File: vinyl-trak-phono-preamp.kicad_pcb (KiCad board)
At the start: 2 copper layers, 64 x 31.5 mm, 67 parts, among them J2 Screw_Terminal_01x03, J3 Screw_Terminal_01x02, J4 Screw_Terminal_01x02, Q1 2N3906, Q10 2N3906, Q11 JFE2140D, Q12 2N5089, Q13 2N3904, Q14 2N3904, Q15 2N5089, Q16 2N5087, Q17 2N5087, Q18 2N5089, Q19 2N5089, Q2 2N3904, Q20 2N5087, Q21 2N5089, Q3 2N3906, Q4 2N3906, Q5 2N3904, Q6 2N3904, Q7 2N3904, Q8 2N3906, Q9 2N3904, U1 OPA2134

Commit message: Revision 0.1
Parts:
- removed J2: Screw_Terminal_01x03, TerminalBlock_4Ucon:TerminalBlock_4Ucon_1x03_P3.50mm_Horizontal
- removed J3: Screw_Terminal_01x02, TerminalBlock_4Ucon:TerminalBlock_4Ucon_1x02_P3.50mm_Horizontal
- removed R38: 1, Resistor_SMD:R_0805_2012Metric_Pad1.20x1.40mm_HandSolder
- added C10: 100p, Capacitor_SMD:C_0805_2012Metric_Pad1.18x1.45mm_HandSolder, F.Cu at (74.9, 96.4)
- added C13: 0.015u, Capacitor_SMD:C_0805_2012Metric_Pad1.18x1.45mm_HandSolder, F.Cu at (104.0, 102.1)
- added C14: .47u, Capacitor_SMD:C_1206_3216Metric_Pad1.33x1.80mm_HandSolder, F.Cu at (129.5, 96.5)
- added C15: 10n, Capacitor_SMD:C_0805_2012Metric_Pad1.18x1.45mm_HandSolder, F.Cu at (125.0, 96.7)
- added C16: 10n, Capacitor_SMD:C_0805_2012Metric_Pad1.18x1.45mm_HandSolder, F.Cu at (129.4, 101.8)
- added C17: 0.020u, Capacitor_SMD:C_0805_2012Metric_Pad1.18x1.45mm_HandSolder, F.Cu at (124.8, 108.4)
- added C19: .47u, Capacitor_SMD:C_1206_3216Metric_Pad1.33x1.80mm_HandSolder, F.Cu at (130.5, 58.7)
- added C20: .47u, Capacitor_SMD:C_1206_3216Metric_Pad1.33x1.80mm_HandSolder, F.Cu at (129.5, 94.0)
- added D3: 1N4148W, Diode_SMD:D_SOD-123F, F.Cu at (132.7, 98.9)
- added D4: 1N4148W, Diode_SMD:D_SOD-123F, F.Cu at (132.8, 101.2)
- added J11: Screw_Terminal_01x02, Library:TerminalBlock_4Ucon_1x02_P5mm_Horizontal, F.Cu at (140.2, 91.6)
- added J12: Screw_Terminal_01x02, Library:TerminalBlock_4Ucon_1x02_P5mm_Horizontal, F.Cu at (75.9, 107.1)
- added J13: Screw_Terminal_01x02, Library:TerminalBlock_4Ucon_1x02_P5mm_Horizontal, F.Cu at (77.0, 71.6)
- added J7: Screw_Terminal_01x02, Library:TerminalBlock_4Ucon_1x02_P5mm_Horizontal, F.Cu at (132.5, 117.7)
- added J8: Screw_Terminal_01x02, Library:TerminalBlock_4Ucon_1x02_P5mm_Horizontal, F.Cu at (76.2, 90.5)
- added Q22: 2N3906, Library:SOT-23_Handsoldering-adjusted-pinout, F.Cu at (107.1, 90.4)
- added Q23: 2N3904, Library:SOT-23_Handsoldering-adjusted-pinout, F.Cu at (109.7, 117.1)
- added Q24: 2N3906, Library:SOT-23_Handsoldering-adjusted-pinout, F.Cu at (108.9, 95.4)
- added Q25: 2N3906, Library:SOT-23_Handsoldering-adjusted-pinout, F.Cu at (109.9, 100.8)
- added Q26: 2N3904, Library:SOT-23_Handsoldering-adjusted-pinout, F.Cu at (109.7, 104.4)
- added Q27: 2N3904, Library:SOT-23_Handsoldering-adjusted-pinout, F.Cu at (109.7, 112.0)
- added Q28: 2N3904, Library:SOT-23_Handsoldering-adjusted-pinout, F.Cu at (116.0, 98.0)
- added Q29: 2N3906, Library:SOT-23_Handsoldering-adjusted-pinout, F.Cu at (109.7, 108.2)
- added Q30: 2N3904, Library:SOT-23_Handsoldering-adjusted-pinout, F.Cu at (118.6, 91.7)
- added Q31: 2N3906, Library:SOT-23_Handsoldering-adjusted-pinout, F.Cu at (119.8, 115.6)
- added Q32: JFE2140D, Package_SO:SOIC-8_3.9x4.9mm_P1.27mm, F.Cu at (83.0, 105.6)
- added Q33: 2N5089, Library:SOT-23_Handsoldering-adjusted-pinout, F.Cu at (91.9, 96.7)
- added Q34: 2N3904, Library:SOT-23_Handsoldering-adjusted-pinout, F.Cu at (90.4, 117.1)
- added Q35: 2N3904, Library:SOT-23_Handsoldering-adjusted-pinout, F.Cu at (85.0, 113.0)
- added Q36: 2N5089, Library:SOT-23_Handsoldering-adjusted-pinout, F.Cu at (92.4, 104.2)
- added Q37: 2N5087, Library:SOT-23_Handsoldering-adjusted-pinout, F.Cu at (98.3, 95.5)
- added Q38: 2N5087, Library:SOT-23_Handsoldering-adjusted-pinout, F.Cu at (98.3, 105.6)
- added Q39: 2N5089, Library:SOT-23_Handsoldering-adjusted-pinout, F.Cu at (98.3, 113.2)
- added Q40: 2N5089, Library:SOT-23_Handsoldering-adjusted-pinout, F.Cu at (98.3, 109.4)
- added Q41: 2N5087, Library:SOT-23_Handsoldering-adjusted-pinout, F.Cu at (98.3, 101.8)
- added Q42: 2N5089, Library:SOT-23_Handsoldering-adjusted-pinout, F.Cu at (103.3, 106.9)
- added R32: 100k, Resistor_SMD:R_0805_2012Metric_Pad1.20x1.40mm_HandSolder, F.Cu at (82.0, 100.7)
- added R39: 18k, Resistor_SMD:R_0805_2012Metric_Pad1.20x1.40mm_HandSolder, F.Cu at (74.9, 98.6)
- added R40: 100k, Resistor_SMD:R_0805_2012Metric_Pad1.20x1.40mm_HandSolder, F.Cu at (76.1, 112.2)
- added R41: 1k37, Resistor_SMD:R_0805_2012Metric_Pad1.20x1.40mm_HandSolder, F.Cu at (102.1, 101.8)
- added R42: 205k, Resistor_SMD:R_0805_2012Metric_Pad1.20x1.40mm_HandSolder, F.Cu at (106.0, 103.3)
- added R43: 220, Resistor_SMD:R_0805_2012Metric_Pad1.20x1.40mm_HandSolder, F.Cu at (113.5, 93.9)
- added R44: 220, Resistor_SMD:R_0805_2012Metric_Pad1.20x1.40mm_HandSolder, F.Cu at (113.7, 116.7)
- added R45: 604, Resistor_SMD:R_0805_2012Metric_Pad1.20x1.40mm_HandSolder, F.Cu at (113.5, 90.1)
- added R46: 604, Resistor_SMD:R_0805_2012Metric_Pad1.20x1.40mm_HandSolder, F.Cu at (116.0, 118.1)
- added R47: 1, Resistor_SMD:R_0805_2012Metric_Pad1.20x1.40mm_HandSolder, F.Cu at (116.6, 101.8)
- added R48: 220, Resistor_SMD:R_0805_2012Metric_Pad1.20x1.40mm_HandSolder, F.Cu at (118.6, 101.8)
- added R49: 220, Resistor_SMD:R_0805_2012Metric_Pad1.20x1.40mm_HandSolder, F.Cu at (118.8, 107.8)
- added R50: 1k47, Resistor_SMD:R_0805_2012Metric_Pad1.20x1.40mm_HandSolder, F.Cu at (94.4, 90.4)
- added R52: 100, Resistor_SMD:R_0805_2012Metric_Pad1.20x1.40mm_HandSolder, F.Cu at (88.9, 100.3)
- added R53: 71k5, Resistor_SMD:R_0805_2012Metric_Pad1.20x1.40mm_HandSolder, F.Cu at (90.6, 90.4)
- added R54: 56k2, Resistor_SMD:R_0805_2012Metric_Pad1.20x1.40mm_HandSolder, F.Cu at (81.7, 118.3)
- added R55: 20.5k, Resistor_SMD:R_0805_2012Metric_Pad1.20x1.40mm_HandSolder, F.Cu at (86.8, 90.4)
- added R56: 220, Resistor_SMD:R_0805_2012Metric_Pad1.20x1.40mm_HandSolder, F.Cu at (89.1, 113.2)
- added R57: 160, Resistor_SMD:R_0805_2012Metric_Pad1.20x1.40mm_HandSolder, F.Cu at (86.6, 118.1)
- added R58: 1k47, Resistor_SMD:R_0805_2012Metric_Pad1.20x1.40mm_HandSolder, F.Cu at (98.3, 90.4)
- added R59: 100, Resistor_SMD:R_0805_2012Metric_Pad1.20x1.40mm_HandSolder, F.Cu at (88.1, 106.9)
- added R60: 56k2, Resistor_SMD:R_0805_2012Metric_Pad1.20x1.40mm_HandSolder, F.Cu at (101.0, 98.7)
- added R62: 1k47, Resistor_SMD:R_0805_2012Metric_Pad1.20x1.40mm_HandSolder, F.Cu at (129.8, 105.6)
- added R63: 1k47, Resistor_SMD:R_0805_2012Metric_Pad1.20x1.40mm_HandSolder, F.Cu at (131.8, 105.6)
- added R64: 15k0, Resistor_SMD:R_0805_2012Metric_Pad1.20x1.40mm_HandSolder, F.Cu at (127.8, 107.3)
- added R65: 162k, Resistor_SMD:R_0805_2012Metric_Pad1.20x1.40mm_HandSolder, F.Cu at (124.9, 106.4)
- added R66: 1k78, Resistor_SMD:R_0805_2012Metric_Pad1.20x1.40mm_HandSolder, F.Cu at (97.0, 118.1)
- added R67: 1Meg, Resistor_SMD:R_0805_2012Metric_Pad1.20x1.40mm_HandSolder, F.Cu at (122.0, 102.7)
- added R68: 33.2k, Resistor_SMD:R_0805_2012Metric_Pad1.20x1.40mm_HandSolder, F.Cu at (102.1, 90.4)
- added R69: 3k83, Resistor_SMD:R_0805_2012Metric_Pad1.20x1.40mm_HandSolder, F.Cu at (104.3, 110.8)
- added R70: 47.5k, Resistor_SMD:R_0805_2012Metric_Pad1.20x1.40mm_HandSolder, F.Cu at (100.8, 118.1)
- added R71: 115k, Resistor_SMD:R_0805_2012Metric_Pad1.20x1.40mm_HandSolder, F.Cu at (93.2, 118.3)
- added R72: 1k78, Resistor_SMD:R_0805_2012Metric_Pad1.20x1.40mm_HandSolder, F.Cu at (104.6, 118.1)
- added R75: 1, Resistor_SMD:R_0805_2012Metric_Pad1.20x1.40mm_HandSolder, F.Cu at (105.9, 63.2)
- added R76: 1, Resistor_SMD:R_0805_2012Metric_Pad1.20x1.40mm_HandSolder, F.Cu at (104.8, 98.6)
- added U2: OPA2134, Package_SO:SOIC-8_3.9x4.9mm_P1.27mm, F.Cu at (125.7, 101.5)
- C6: value 1u -> .47u; footprint Capacitor_SMD:C_0805_2012Metric_Pad1.18x1.45mm_HandSolder -> Capacitor_SMD:C_1206_3216Metric_Pad1.33x1.80mm_HandSolder
- D1, D2: value D -> 1N4148W; footprint Diode_SMD:D_0805_2012Metric_Pad1.15x1.40mm_HandSolder -> Diode_SMD:D_SOD-123F
- J4: footprint TerminalBlock_4Ucon:TerminalBlock_4Ucon_1x02_P3.50mm_Horizontal -> Library:TerminalBlock_4Ucon_1x02_P5mm_Horizontal
- R10, R11: value 600 -> 604
- R12, R13: value 215 -> 220
- R16: value 70k -> 71k5
- R23, R24: value 1470 -> 1k47
- R30: value 47k -> 47.5k
- R33: value 20k -> 20.5k
- R34: value 57k -> 56k2
- R35: value 33k -> 33.2k
- R7: value 200k -> 205k
- moved R21 32.5 mm to (102.0, 63.3), turned to 0 degrees
- moved R1 29.6 mm to (83.2, 65.4), turned to 180 degrees
- moved R6 29.5 mm to (103.1, 66.4)
- moved C7 29.5 mm to (126.1, 61.3), turned to 180 degrees
- moved C6 27.2 mm to (130.6, 61.1), turned to 180 degrees
- moved R35 26.4 mm to (103.1, 55.0)
- moved Q16 25.9 mm to (99.3, 60.1), turned to 0 degrees
- moved Q3 25.6 mm to (110.0, 60.0)
- moved Q1 25.4 mm to (108.2, 55.0), turned to 180 degrees
- moved C4 24.8 mm to (105.1, 66.8), turned to 90 degrees
- moved R28 24.4 mm to (123.1, 67.3), turned to -90 degrees
- moved Q9 24.0 mm to (119.6, 56.3), turned to 90 degrees
- moved Q6 23.7 mm to (110.7, 76.6), turned to 0 degrees
- moved R37 23.2 mm to (117.7, 66.4)
- moved Q5 22.8 mm to (110.7, 69.0)
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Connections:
- net /buffer renamed /phono-in-left/buffer
- net /buffer+ renamed /phono-in-left/buffer-
- net /cartridge+ renamed /l-in-
- net /cartridge- renamed /l-in+
- net /cascode renamed /phono-in-left/cascode
- net /out renamed /l-out
- C6 pad 2: Net-(C6-Pad2) -> Net-(C19-Pad2)
- Q11 pad 1: Net-(Q11C-VCH) -> Net-(Q14-C)
- Q11 pad 3: Net-(Q11C-VCH) -> unconnected-(Q11C-VCH-Pad3)
- Q11 pad 5: Net-(Q11C-VCH) -> Net-(Q14-C)
- Q11 pad 7: Net-(Q11C-VCH) -> unconnected-(Q11C-VCL-Pad7)
- Q12 pad 1: /buffer- -> /phono-in-left/buffer+
- Q14 pad 1: Net-(Q11C-VCH) -> Net-(Q14-C)
- Q16 pad 3: /buffer- -> /phono-in-left/buffer+
- R14 pad 2: Net-(R14-Pad2) -> /phono-in-left/buffer+
- R21 pad 2: Net-(C6-Pad2) -> Net-(R21-Pad2)
- U1 pad 7: Net-(C6-Pad2) -> Net-(C19-Pad2)
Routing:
- net -15: track 152.0 -> 247.5 mm, vias 1 -> 0
- net Net-(Q33-B): track 0.00 -> 34.7 mm
- net Net-(Q37-B): track 0.00 -> 34.2 mm
- net Net-(C19-Pad2): track 0.00 -> 33.1 mm
- net Net-(C14-Pad2): track 0.00 -> 33.1 mm
- net Net-(Q34-C): track 0.00 -> 32.9 mm
- net /phono-in-left/cascode: track 57.1 -> 27.6 mm
- net /phono-in-right/cascode: track 0.00 -> 27.7 mm
- net +15V: track 138.6 -> 165.8 mm, vias 0 -> 1
- net /r-in-: track 0.00 -> 26.3 mm
- net /phono-in-right/buffer-: track 0.00 -> 20.4 mm
- net Net-(Q25-C): track 0.00 -> 20.3 mm
- net Net-(Q11C-VCH): track 19.3 -> 0.00 mm
- net /phono-in-right/buffer: track 0.00 -> 18.6 mm
- net Net-(Q27-C): track 0.00 -> 18.0 mm
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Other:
- board size 64 x 31.5 mm -> 75 x 75 mm
- board text added: "+15 -15"
- board text added: "VinylTrak MM Phono Preamp Input Stage - Rev. 0.1 Designed by Bob Cordell Created by Brian Lubeski • 2026-05"
- board text added: "gnd"
- board text added: "left: in+ in-"
- board text added: "left: out- out+"
- board text added: "right: in+ in-"
- board text added: "right: out- out+"
- board text removed: "+in -in"
- board text removed: "-15 +15 GND"
- board text removed: "-out +out"

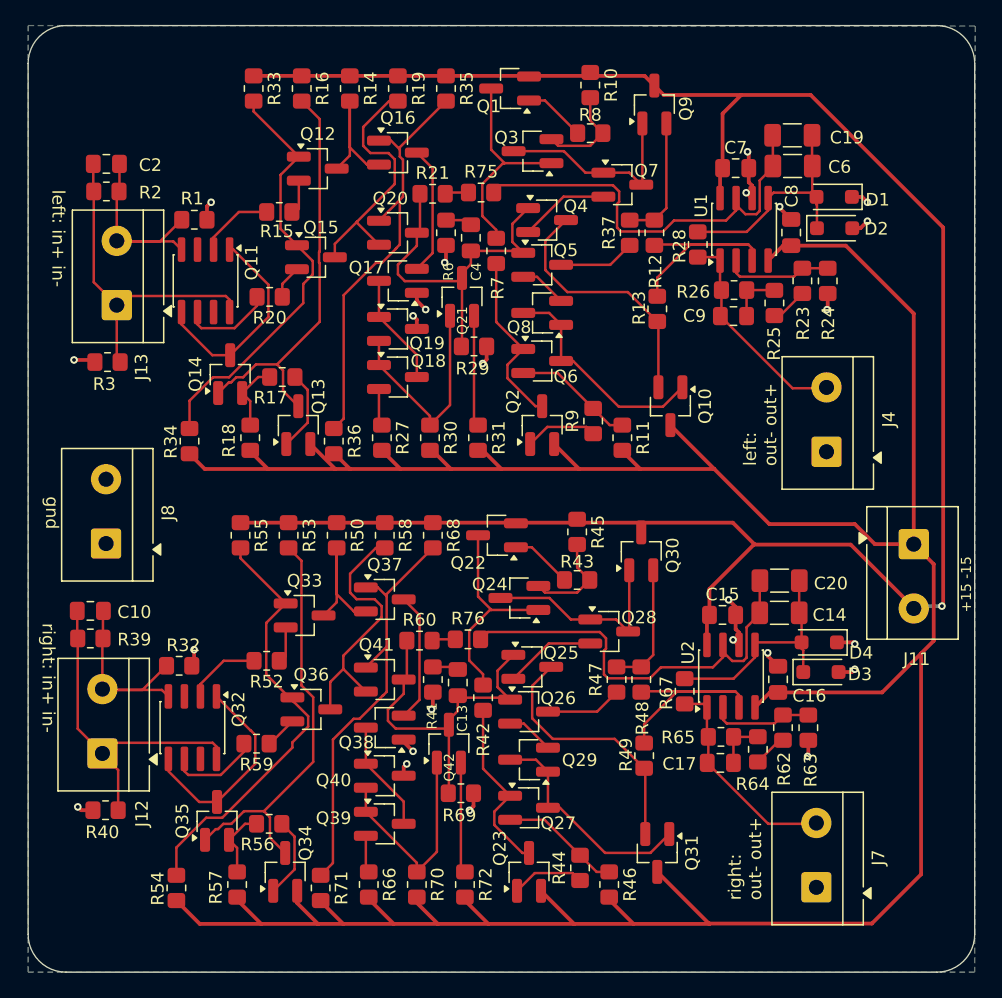
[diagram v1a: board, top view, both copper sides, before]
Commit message: Revision 0.2
- TH components mounted to PCB back to preserve front space
- 15+ and 15- lines are kept closer together to reduce noise (even though di/dt is relatively low)
- Signal path bends around PCB area; DC servo feedback path is much shorter
- Signal path kept on first layer without jumpers

- Power distribution is messy
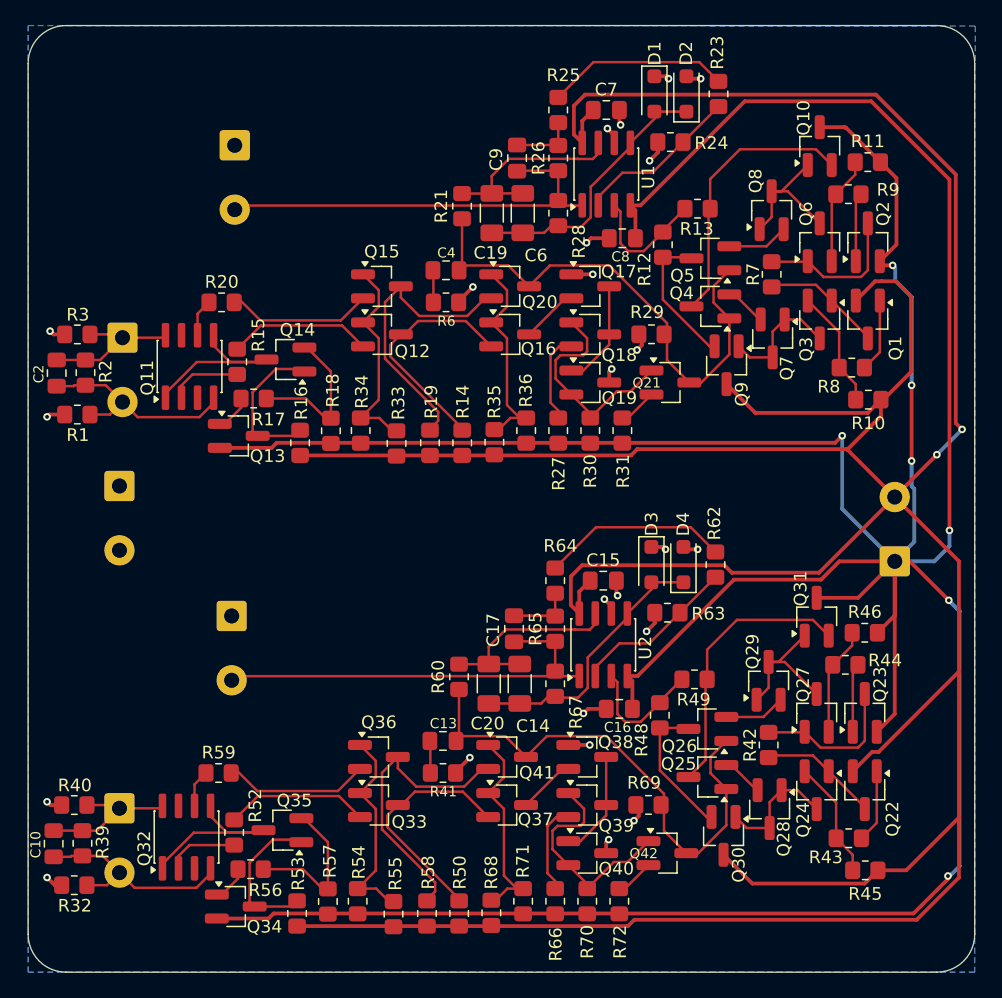
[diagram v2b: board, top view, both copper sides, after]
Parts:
- removed J12, J13, J4, J7: Screw_Terminal_01x02, Library:TerminalBlock_4Ucon_1x02_P5mm_Horizontal
- removed R37, R47, R75, R76: 1, Resistor_SMD:R_0805_2012Metric_Pad1.20x1.40mm_HandSolder
- added J14: Screw_Terminal_01x02, Library:TerminalBlock_4Ucon_1x02_P5mm_Horizontal, B.Cu at (77.5, 75.3)
- added J15: Screw_Terminal_01x02, Library:TerminalBlock_4Ucon_1x02_P5mm_Horizontal, B.Cu at (77.2, 112.5)
- added J16: Screw_Terminal_01x02, Library:TerminalBlock_4Ucon_1x02_P5mm_Horizontal, B.Cu at (86.4, 60.0)
- added J17: Screw_Terminal_01x02, Library:TerminalBlock_4Ucon_1x02_P5mm_Horizontal, B.Cu at (86.1, 97.3)
- D1, D2, D3, D4: value 1N4148W -> D
- J11, J8: moved to B.Cu
- moved Q22 35.5 mm to (136.3, 110.6), turned to -90 degrees
- moved R45 35.2 mm to (136.3, 116.9), turned to 180 degrees
- moved Q1 33.7 mm to (136.5, 73.3), turned to -90 degrees
- moved R10 33.3 mm to (136.6, 79.6), turned to 180 degrees
- moved R55 32.4 mm to (99.0, 120.4), turned to 90 degrees
- moved R50 31.5 mm to (104.2, 120.3), turned to 90 degrees
- moved R33 30.3 mm to (99.2, 83.1), turned to 90 degrees
- moved R68 30.3 mm to (106.7, 120.3), turned to 90 degrees
- moved R58 30.1 mm to (101.6, 120.3), turned to 90 degrees
- moved R53 30.0 mm to (91.3, 120.3), turned to 90 degrees
- moved R43 29.7 mm to (135.0, 114.4), turned to 180 degrees
- moved Q2 29.6 mm to (136.5, 67.2)
- moved R14 29.5 mm to (104.4, 83.1), turned to 90 degrees
- moved Q23 29.4 mm to (136.3, 104.5)
- moved R11 29.2 mm to (136.5, 60.8), turned to 0 degrees
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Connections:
- net +15V renamed 15+
- net -15 renamed 15-
- Q30 pad 3: Net-(Q30-E) -> Net-(Q26-C)
- Q9 pad 3: Net-(Q9-E) -> Net-(Q5-C)
- R12 pad 1: Net-(Q9-E) -> Net-(Q5-C)
- R21 pad 2: Net-(R21-Pad2) -> Net-(C19-Pad2)
- R48 pad 1: Net-(Q30-E) -> Net-(Q26-C)
- R60 pad 2: Net-(R60-Pad2) -> Net-(C14-Pad2)
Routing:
- net 15+: track 165.8 -> 304.3 mm, vias 1 -> 2
- net 15-: track 247.5 -> 312.8 mm, vias 0 -> 7
- net Net-(Q34-C): track 32.9 -> 11.2 mm
- net Net-(Q13-C): track 32.5 -> 11.2 mm
- net Net-(C19-Pad2): track 33.1 -> 14.5 mm
- net Net-(C14-Pad2): track 33.1 -> 14.5 mm
- net Net-(Q16-B): track 34.4 -> 15.9 mm
- net Net-(Q37-B): track 34.2 -> 15.9 mm
- net Net-(Q33-B): track 34.7 -> 16.4 mm
- net Net-(Q12-B): track 33.9 -> 16.4 mm
- net /r-out: track 16.8 -> 33.2 mm
- net /l-out: track 16.8 -> 33.2 mm
- net /r-in-: track 26.3 -> 11.5 mm
- net /l-in-: track 24.9 -> 11.5 mm
- net /phono-in-left/cascode: track 27.6 -> 40.5 mm
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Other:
- board text added: "VinylTrak MM Phono Preamp Input Stage - Rev. ${REV} Designed by Bob Cordell Created by Brian Lubeski • 2026-05"
- board text added: "out+ out- left:"
- board text added: "out+ out- right:"
- board text removed: "VinylTrak MM Phono Preamp Input Stage - Rev. 0.1 Designed by Bob Cordell Created by Brian Lubeski • 2026-05"
- board text removed: "left: out- out+"
- board text removed: "right: out- out+"

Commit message: Revision 0.3 - Fix reverse-wired DC servo - Reduce gain from 40 db to 35 db
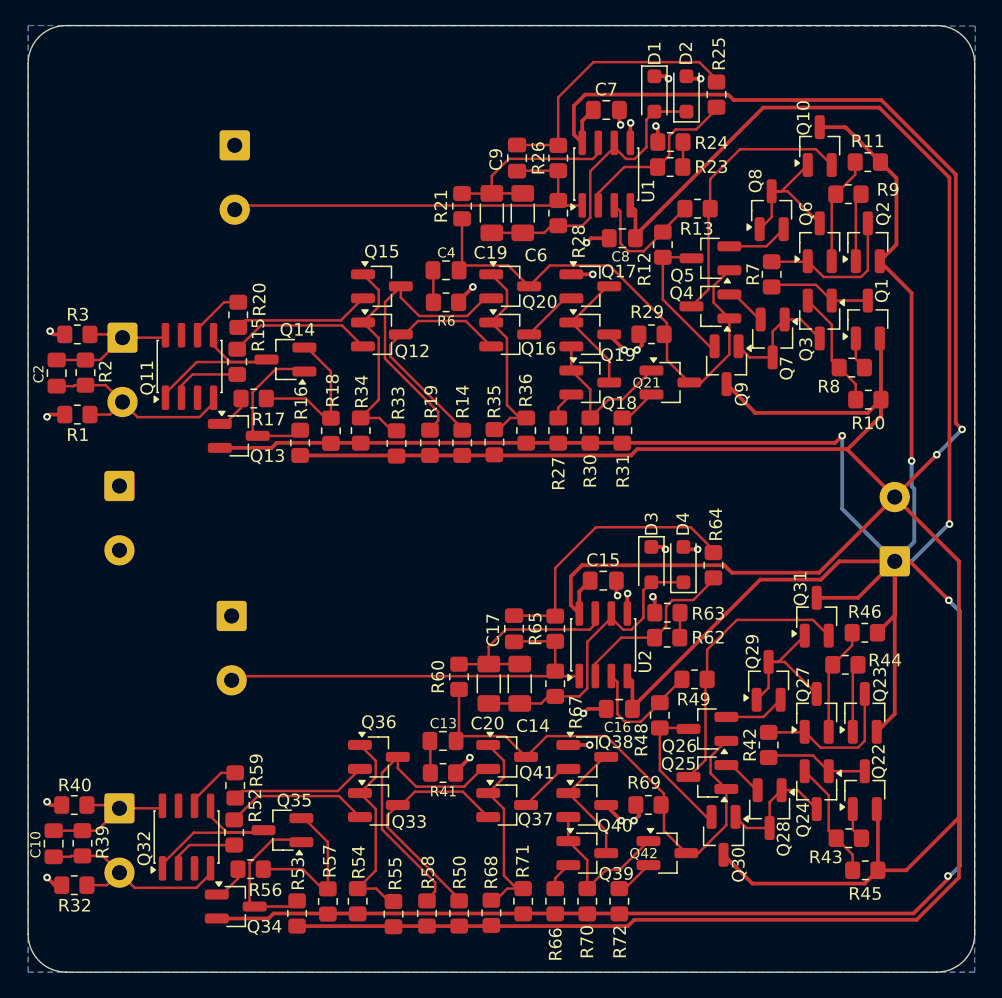
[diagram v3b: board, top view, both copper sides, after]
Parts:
- moved R25 12.6 mm to (124.5, 55.5), turned to 90 degrees
- moved R64 12.6 mm to (124.3, 92.8), turned to 90 degrees
- moved R23 6.94 mm to (120.9, 61.2), turned to 180 degrees
- moved R62 6.94 mm to (120.6, 98.5), turned to 180 degrees
- moved Q18 3.81 mm to (114.5, 78.3)
- moved Q19 3.81 mm to (114.5, 74.5)
- moved Q39 3.81 mm to (114.3, 115.6)
- moved Q40 3.81 mm to (114.3, 111.8)
- moved R20 1.65 mm to (86.6, 72.9), turned to 90 degrees
- moved R59 1.65 mm to (86.4, 110.2), turned to 90 degrees
- turned Q1 to 90 degrees
- turned Q22 to 90 degrees
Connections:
- R23 pad 1: Net-(U1A--) -> Net-(R23-Pad1)
- R23 pad 2: Net-(R23-Pad2) -> Net-(U1A--)
- R24 pad 2: Net-(U1A--) -> Net-(R23-Pad1)
- R25 pad 1: Net-(R23-Pad2) -> Net-(U1A--)
- R62 pad 1: Net-(U2A--) -> Net-(R62-Pad1)
- R62 pad 2: Net-(R62-Pad2) -> Net-(U2A--)
- R63 pad 2: Net-(U2A--) -> Net-(R62-Pad1)
- R64 pad 1: Net-(R62-Pad2) -> Net-(U2A--)
- U1 pad 5: Net-(D1-A) -> 0
- U1 pad 6: 0 -> Net-(D1-A)
- U2 pad 5: Net-(D3-A) -> 0
- U2 pad 6: 0 -> Net-(D3-A)
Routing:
- net Net-(C17-Pad2): track 5.03 -> 21.9 mm
- net 15+: track 304.3 -> 287.5 mm
- net Net-(C9-Pad2): track 5.03 -> 21.5 mm
- net Net-(R62-Pad2): track 14.8 -> 0.00 mm
- net Net-(R23-Pad2): track 14.5 -> 0.00 mm
- net Net-(Q39-E): track 7.16 -> 2.29 mm
- net Net-(Q18-E): track 7.16 -> 2.29 mm
- net Net-(Q18-B): track 17.4 -> 12.7 mm
- net Net-(Q39-B): track 17.4 -> 12.7 mm
- net Net-(Q1-B): track 5.82 -> 2.59 mm
- net Net-(Q22-B): track 5.82 -> 2.59 mm
- net Net-(D3-A): track 19.3 -> 22.4 mm
- net Net-(D1-A): track 19.3 -> 22.4 mm
- net Net-(R62-Pad1): track 0.00 -> 1.96 mm
- net Net-(R23-Pad1): track 0.00 -> 1.96 mm
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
